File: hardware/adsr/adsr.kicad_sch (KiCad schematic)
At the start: 87 parts, among them J1 MonoJack, J2 MonoJack, J3 MonoJack, J4 Conn_02x05_Odd_Even, Q1 BC847, Q2 BC847, Q3 BC847, Q4 BC847, Q5 BC847, Q6 BC847, Q7 BC847, Q8 2N7002K, Q9 BC847, SW1 SW_Push, SW2 SW_DPDT_x2, U1 TLC555xD, U2 HEF4093B, U3 TLC555xD, U4 TL074

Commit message: routed PCB, needs cleanup
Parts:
- RV1, RV2, RV3, RV4, RV5: footprint Potentiometer_THT:Potentiometer_Bourns_PTV09A-1_Single_Vertical -> Audio_Potentiometer_THT:Potentiometer_Bourns_PTV09A-1_Single_Vertical_thin
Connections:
- net NRESET: now also U4.10 (+); no longer U4.12 (+)
- net at D2.1 (K), R3.2, R4.1: now also SW2.6 (C); no longer SW2.1 (A)
- net at R23.1, R25.1, R26.2: now also U4.12 (+); no longer U4.10 (+)
- net NTRIG: now reaches D4.2 (A), Q6.3 (C), R18.2, U3.2 (TR)
- net QOUT: now reaches R22.2, U3.3 (Q)
- net QOUT: now also D9.2 (A); no longer R28.1
- net THR: now reaches C8.1, RV4.3, RV5.3, U3.6 (THR), U4.3 (+)
- net THR: now also RV3.3; no longer D9.1 (K)
- net at U1.2 (TR): now also SW2.2 (B); no longer SW2.5 (B)
- net at Q2.1 (B): now also SW2.5 (B); no longer SW2.2 (B)
- net at SW2.3 (C): now also R17.2; no longer R7.1
- net at SW2.4 (A): now also R7.1; no longer R17.2
- net at Q7.3 (C), R20.2: now also SW2.1 (A); no longer SW2.6 (C)
- net at D7.2 (A), R29.1: now also U4.9 (-); no longer U4.13 (-)
- net at D7.1 (K): now also U4.8; no longer U4.14
- net at Q9.1 (B), R31.1, U4.1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: now also U4.13 (-); no longer U4.9 (-)
- net ENDOF: now reaches R21.2, R23.2
- net ENDOF: now also U4.14; no longer U4.8
- new net: D9.1 (K), R28.1
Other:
- moved on the sheet: D9, Q7, R20, R21, R28, RV3, SW2A, SW2B, U4C, U4D

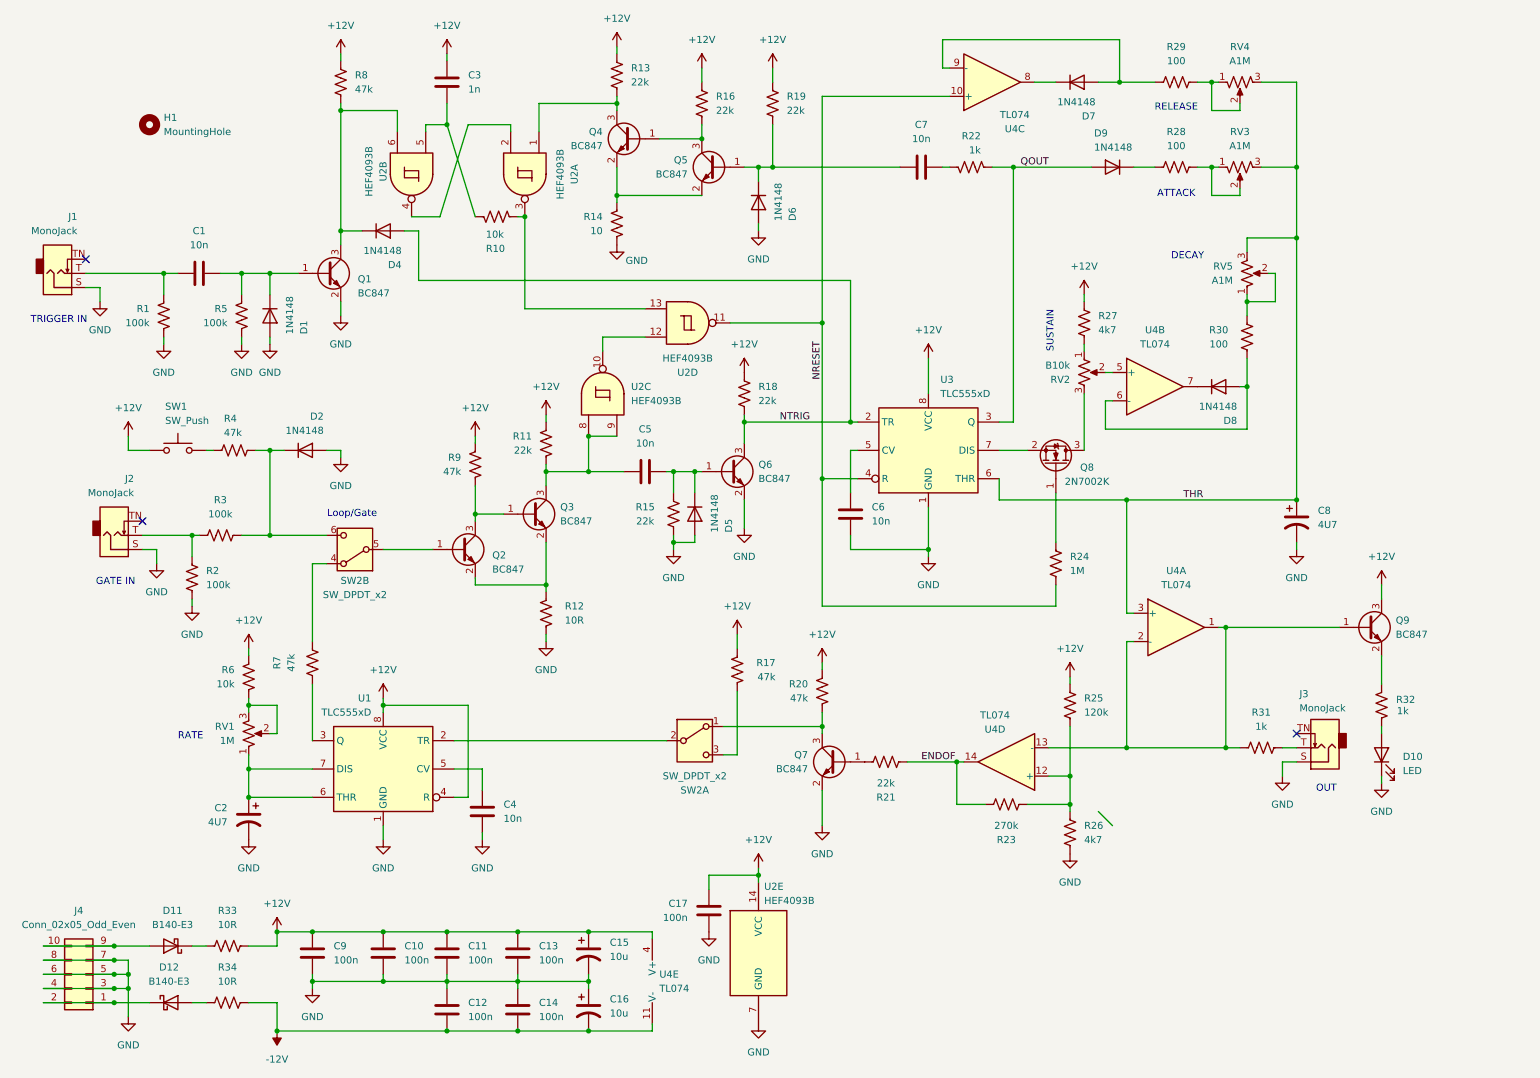
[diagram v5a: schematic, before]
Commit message: clean up silk, check board, generate gerbers for v2
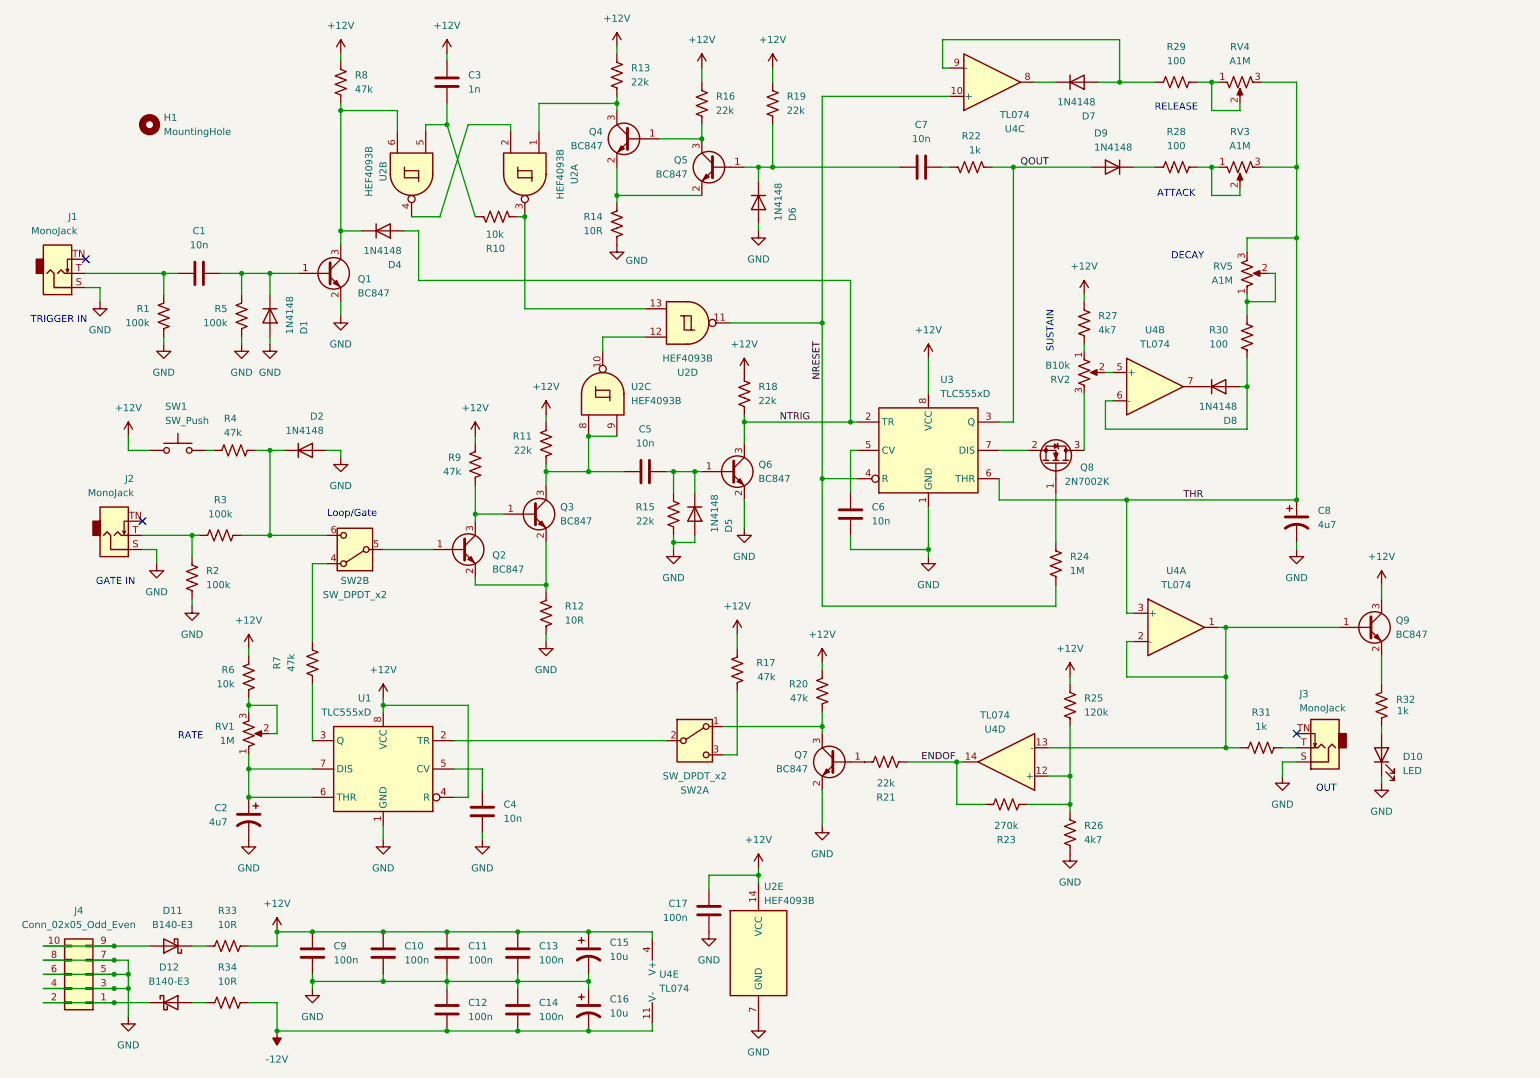
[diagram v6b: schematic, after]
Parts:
- C2, C8: value 4U7 -> 4u7
- R14: value 10 -> 10R
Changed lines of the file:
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@@
 	(title_block
 		(title "ADSR EG")
-		(date "2025-11-16")
+		(date "2025-11-23")
 		(rev "2.0")
 		(company "idyllm")
@@
 	)
 	(junction
-		(at 212.09 146.05)
-		(diameter 0)
-		(color 0 0 0 0)
-	)
-	(junction
 		(at 157.48 69.85)
 		(diameter 0)
@@
 	)
 	(junction
+		(at 229.87 133.35)
+		(diameter 0)
+		(color 0 0 0 0)
+	)
+	(junction
 		(at 134.62 96.52)
 		(diameter 0)
@@
 		(at 35.56 105.41)
 	)
-	(bus_entry
-		(at 207.01 157.48)
-		(size 2.54 2.54)
-		(stroke
-			(width 0)
-			(type default)
-		)
-	)
 	(wire
 		(pts
@@
 	(wire
 		(pts
-			(xy 198.12 146.05) (xy 212.09 146.05)
+			(xy 198.12 146.05) (xy 229.87 146.05)
 		)
 		(stroke
@@
 	(wire
 		(pts
-			(xy 212.09 146.05) (xy 229.87 146.05)
+			(xy 212.09 133.35) (xy 229.87 133.35)
 		)
 		(stroke
@@
 	(wire
 		(pts
-			(xy 212.09 127) (xy 212.09 146.05)
+			(xy 212.09 127) (xy 212.09 133.35)
 		)
 		(stroke
@@
 	(wire
 		(pts
+			(xy 229.87 133.35) (xy 229.87 124.46)
+		)
+		(stroke
+			(width 0)
+			(type default)
+		)
+	)
+	(wire
+		(pts
 			(xy 120.65 46.99) (xy 120.65 48.26)
 		)
@@
 	(wire
 		(pts
-			(xy 229.87 146.05) (xy 229.87 124.46)
+			(xy 229.87 146.05) (xy 229.87 133.35)
 		)
 		(stroke
@@
 			)
 		)
-		(property "Value" "10"
+		(property "Value" "10R"
 			(at 118.11 53.3399 0)
 			(effects
@@
 			)
 		)
-		(property "Value" "4U7"
+		(property "Value" "4u7"
 			(at 50.8 159.3849 0)
 			(effects
@@
 			)
 		)
-		(property "Value" "4U7"
+		(property "Value" "4u7"
 			(at 246.38 106.0449 0)
 			(effects
